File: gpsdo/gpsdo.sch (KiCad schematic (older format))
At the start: 1 part

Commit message: main
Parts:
- added C? (x11): 100n, Capacitor_SMD:C_0402_1005Metric, symbol pace:100n
- added C? (x2): 10u, Capacitor_SMD:C_0402_1005Metric, symbol pace:10u
- added F?: fuse-250mA, Fuse:Fuse_1206_3216Metric, symbol pace:fuse-250mA
- added FB? (x2): bead, Inductor_SMD:L_0805_2012Metric, symbol pace:bead
- added H? (x4): MountingHole_Pad, MountingHole:MountingHole_3.2mm_M3_Pad, symbol pace:MountingHole_Pad
- added J?: Barrel_Jack_Switch, Connector_BarrelJack:BarrelJack_Horizontal, symbol pace:Barrel_Jack_Switch
- added J?: USB_B_Micro, Connector_USB:USB_Micro-B_Molex-105017-0001, symbol pace:USB_B_Micro
- added J?: Conn_01x02_Male, symbol Connector:Conn_01x02_Male
- added J?: Conn_02x05_Odd_Even, symbol Connector_Generic:Conn_02x05_Odd_Even
- added R? (x2): 100k, Resistor_SMD:R_0402_1005Metric, symbol pace:100k
- added SW?: pushbutton_switch, Button_Switch_THT:SW_PUSH_6mm, symbol pace:pushbutton_switch
- added SW?: SW_SPDT, pace:Switch_Toggle_ATE1D-2M3-10-Z, symbol pace:SW_SPDT
- added U?: AP1117-33, Package_TO_SOT_SMD:SOT-223-3_TabPin2, symbol pace:AP1117-33
- added U?: SRV05-4, Package_TO_SOT_SMD:SOT-23-6, symbol pace:SRV05-4
- added U?: 74AHC1G04, Package_TO_SOT_SMD:SOT-353_SC-70-5, symbol pace:74AHC1G04
- added X?: AOCJY1-10.000MHZ, Oscillator:Oscillator_DIP-14, symbol pace:AOCJY1-10.000MHZ
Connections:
- net GND: now reaches U?.10 (VSS)
- net GND: now also U?.20 (VSSA), U?.27 (VSS), U?.74 (VSS), U?.99 (VSS), C?.2, C?.2, C?.2, C?.2, C?.2, C?.2, C?.2, C?.2, C?.2, C?.2, C?.2, C?.2, C?.2, H?.1, H?.1, H?.1, H?.1, J?.1 (Pin_1), J?.2, J?.3, J?.5 (GND), R?.2, SW?.1, U?.1 (GND), U?.2 (VN), U?.3 (GND), X?.7 (GND)
- net +3V3: now reaches U?.100 (VDD)
- net +3V3: now also U?.11 (VDD), U?.19 (VDD), U?.28 (VDD), U?.50 (VDD), U?.6 (VBAT), U?.75 (VDD), C?.1, C?.1, C?.1, C?.1, C?.1, C?.1, C?.1, C?.1, C?.1, C?.1, FB?.1, U?.2 (VO), U?.5 (VCC), X?.14 (Vcc)
- net at U?.22 (VDDA): now also C?.1, FB?.2
- new net: J?.1, SW?.2 (B)
- new net: F?.2, SW?.1 (A)
- new net: C?.1, FB?.1, U?.3 (VI)
- new net: F?.1, FB?.2
- new net: J?.2 (Pin_2), U?.4
- new net OSC_10MHZ: U?.2, X?.8 (OUT)
- new net OSC_CONTROL: X?.1 (Vcontrol)
- new net USB_DM: J?.2 (D-), U?.3 (IO2)
- new net USB_DP: J?.3 (D+), U?.1 (IO1)
- new net VUSB: J?.1 (VBUS), R?.1, U?.5 (VP)
- new net VUSB_SENSE: R?.1, R?.2
- new net nRESET: C?.1, SW?.2
- no-connect marks 0 -> 4
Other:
- moved on the sheet: U?

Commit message: layout
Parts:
- added AE1: Antenna_Shield, pace:sma, symbol Device:Antenna_Shield
- added C10, C15: 100n, Capacitor_SMD:C_0402_1005Metric, symbol pace:100n
- added C16, C17: 2.2uF, Capacitor_SMD:C_0603_1608Metric, symbol pace:2.2uF
- added D1: ledgreen, LED_SMD:LED_0603_1608Metric, symbol pace:ledgreen
- added D2: SS210, Diode_SMD:D_SMA, symbol pace:SS210
- added J3: Conn_01x04_Male, Connector_PinHeader_2.54mm:PinHeader_1x04_P2.54mm_Vertical, symbol Connector:Conn_01x04_Male
- added J6: Conn_01x06_Male, Connector_PinHeader_2.54mm:PinHeader_1x06_P2.54mm_Vertical, symbol Connector:Conn_01x06_Male
- added L1: 47nH, Inductor_SMD:L_0603_1608Metric, symbol pace:47nH
- added R1, R2, R3, R4, R5, R6: 10k, Resistor_SMD:R_0402_1005Metric, symbol pace:10k
- added TH1: 47k, Resistor_SMD:R_0603_1608Metric, symbol pace:47k
- added TP1, TP2, TP3: TestPoint, TestPoint:TestPoint_Pad_D1.0mm, symbol pace:TestPoint
- added U2: ATGM336H-5N, pace:module18_9.7x10.1mm_P1.1mm, symbol pace:ATGM336H-5N
- J1: renamed from J?; footprint (none) -> Connector_PinHeader_1.27mm:PinHeader_2x05_P1.27mm_Vertical
- J5: renamed from J?; footprint (none) -> Connector_PinHeader_2.54mm:PinHeader_1x02_P2.54mm_Vertical
- gave numbers to parts that had none: 31
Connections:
- net +3V3: now also J1.1 (Pin_1), C15.1, J3.2 (Pin_2), R2.1, R3.1, R4.1, U2.8 (VCC)
- net GND: now also J1.3 (Pin_3), J1.5 (Pin_5), J1.9 (Pin_9), AE1.2 (Shield), C10.2, C15.2, C16.2, C17.2, D1.1 (K), J3.1 (Pin_1), J6.1 (Pin_1), R1.2, TH1.2, U2.1 (GND), U2.10 (GND), U2.12 (GND)
- net OSC_10MHZ: now also U1.12 (PH0), U1.31 (PA6), U1.40 (PE9), TP2.1
- net OSC_CONTROL: now also U1.29 (PA4), R6.1, TP1.1; no longer X1.1 (Vcontrol)
- net USB_DM: now also U1.70 (PA11)
- net USB_DP: now also U1.71 (PA12)
- net VUSB_SENSE: now also U1.68 (PA9)
- net nRESET: now also J1.10 (Pin_10), U1.14 (NRST)
- net GPS_1PPS: now reaches U1.32 (PA7)
- net GPS_1PPS: now also U1.42 (PE11), TP3.1, U2.4 (1PPS)
- net GPS_ONOFF: now reaches U1.35 (PB0)
- net GPS_ONOFF: now also U2.5 (ONOFF)
- net GPS_nRESET: now reaches U1.36 (PB1)
- net GPS_nRESET: now also U2.9 (nRESET)
- net LED_STATUS: now reaches U1.37 (PB2)
- net LED_STATUS: now also R5.1
- net CPU_TO_GPS: now reaches U1.47 (PB10)
- net CPU_TO_GPS: now also U2.3 (RXD)
- net GPS_TO_CPU: now reaches U1.48 (PB11)
- net GPS_TO_CPU: now also U2.2 (TXD)
- net at U1.49 (VCAP_1): now also C16.1
- net CPU_TO_AUX: now reaches U1.63 (PC6)
- net CPU_TO_AUX: now also J6.5 (Pin_5)
- net AUX_TO_CPU: now reaches U1.64 (PC7)
- net AUX_TO_CPU: now also J6.4 (Pin_4)
- net SWDIO: now reaches U1.72 (PA13)
- net SWDIO: now also J1.2 (Pin_2)
- net at U1.73 (VCAP_2): now also C17.1
- net SWDCLK: now reaches U1.76 (PA14)
- net SWDCLK: now also J1.4 (Pin_4)
- net SWO: now reaches U1.89 (PB3)
- net SWO: now also J1.6 (Pin_6)
- net SDA: now reaches U1.93 (PB7)
- net SDA: now also J3.4 (Pin_4), R3.2, U2.16 (SDA)
- net BOOT0: now reaches U1.94 (BOOT0)
- net BOOT0: now also R1.1
- net SCL: now reaches U1.95 (PB8)
- net SCL: now also J3.3 (Pin_3), R2.2, U2.17 (SCL)
- net at J2.1: now also D2.2 (A); no longer SW2.2 (B)
- new net: AE1.1 (A), L1.2, U2.11 (RF_IN)
- new net: L1.1, U2.14 (VCC_RF)
- new net: C10.1, R6.2, X1.1 (Vcontrol)
- new net: D2.1 (K), SW2.2 (B)
- new net: D1.2 (A), R5.2
- new net BOARD_TEMP: R4.2, TH1.1
- no-connect marks 4 -> 73
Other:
- note added: "5..12v"
- note added: "Max input 15v"
- note added: "TC = 1 msec"
- moved on the sheet: C12, C14, J1, J2, J4, J5, R7, R8, U4, U5, X1

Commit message: layout
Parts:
- removed D1: ledgreen, LED_SMD:LED_0603_1608Metric, symbol pace:ledgreen
- removed J3: Conn_01x04_Male, Connector_PinHeader_2.54mm:PinHeader_1x04_P2.54mm_Vertical, symbol Connector:Conn_01x04_Male
- removed J6: Conn_01x06_Male, Connector_PinHeader_2.54mm:PinHeader_1x06_P2.54mm_Vertical, symbol Connector:Conn_01x06_Male
- removed U4: 74AHC1G04, Package_TO_SOT_SMD:SOT-353_SC-70-5, symbol pace:74AHC1G04
- removed U5: SRV05-4, Package_TO_SOT_SMD:SOT-23-6, symbol pace:SRV05-4
- added AE2, AE3, AE4, AE5, AE6, AE7, AE8, AE9: Antenna_Shield, pace:sma, symbol Device:Antenna_Shield
- added C18, C19: 12pf, Capacitor_SMD:C_0402_1005Metric, symbol pace:12pf
- added D1: ledgreen_0805, LED_SMD:LED_0805_2012Metric, symbol pace:ledgreen_0805
- added R9: 220, Resistor_SMD:R_0402_1005Metric, symbol pace:220
- added U4: 74AHC1G04-newfp, pace:SOT-70-dck, symbol pace:74AHC1G04-newfp
- added U5: SRV05-4-newfp, pace:srv05-4, symbol pace:SRV05-4-newfp
- added Y1: 16mhz, Crystal:Crystal_SMD_3225-4Pin_3.2x2.5mm, symbol pace:16mhz
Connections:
- net +3V3: now also U4.5 (VCC)
- net BOARD_TEMP: now also U1.25 (PA2)
- net GND: now also AE2.2 (Shield), AE3.2 (Shield), AE4.2 (Shield), AE5.2 (Shield), AE6.2 (Shield), AE7.2 (Shield), AE8.2 (Shield), AE9.2 (Shield), C18.2, C19.2, D1.1 (K), U4.3 (GND), U5.2 (VN), Y1.2, Y1.4
- net GPS_1PPS: now also U1.69 (PA10); no longer U1.42 (PE11)
- net LED_STATUS: now also U1.26 (PA3); no longer U1.37 (PB2)
- net OSC_10MHZ: now also U1.67 (PA8), U1.90 (PB4), U4.2; no longer U1.12 (PH0), U1.31 (PA6), U1.40 (PE9)
- net USB_DM: now also U5.4 (IO3)
- net USB_DP: now also U5.3 (IO2)
- net VUSB: now also U5.5 (VP)
- net at U1.13 (PH1): now also R9.1
- net at R5.2: now also D1.2 (A)
- net at J5.2 (Pin_2): now also U4.4
- net AUX_TO_CPU: no longer names the net of U1.64 (PC7)
- net CPU_TO_AUX: no longer names the net of U1.63 (PC6)
- new net: C18.1, U1.12 (PH0), Y1.1
- new net: C19.1, R9.2, Y1.3
- new net: AE4.1 (A), AE8.1 (A)
- new net: AE5.1 (A), AE9.1 (A)
- new net: AE3.1 (A), AE7.1 (A)
- new net: AE2.1 (A), AE6.1 (A)
- no-connect marks 73 -> 70
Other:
- note added: "use JLC7628 ; 50 ohm trace = 11.55 mil"
- moved on the sheet: AE1, C15, L1, U2

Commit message: rotate
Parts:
- U5: footprint pace:srv05-4 -> pace:SOT-23-6L-srv05
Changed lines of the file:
@@
 F 0 "U5" H 8650 2631 50  0000 C CNN
 F 1 "SRV05-4-newfp" H 8650 2540 50  0000 C CNN
-F 2 "pace:srv05-4" H 9350 1500 50  0001 C CNN
+F 2 "pace:SOT-23-6L-srv05" H 9350 1500 50  0001 C CNN
 F 3 "http://www.onsemi.com/pub/Collateral/SRV05-4-D.PDF" H 8650 1950 50  0001 C CNN
 F 4 "C85364" H 8650 1950 50  0001 C CNN "LCSC"

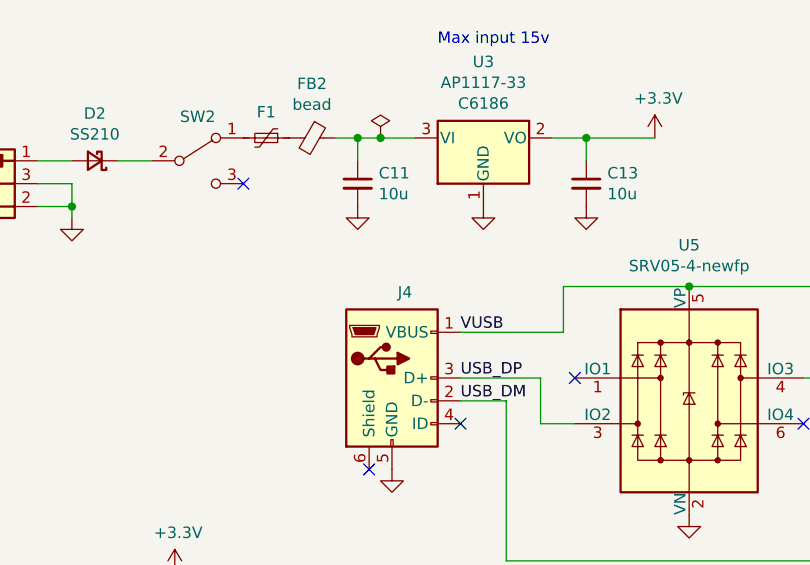
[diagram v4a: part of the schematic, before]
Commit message: usb connector
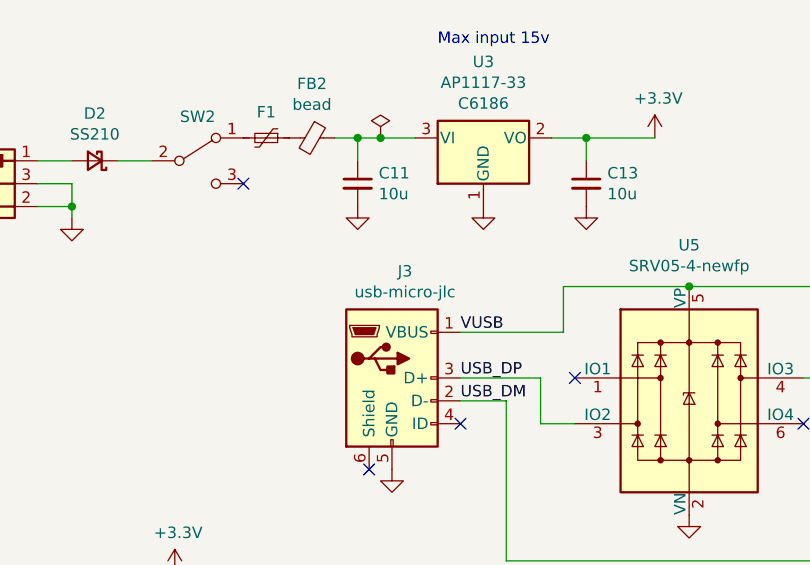
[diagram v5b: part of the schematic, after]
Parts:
- removed J4: USB_B_Micro, Connector_USB:USB_Micro-B_Molex-105017-0001, symbol pace:USB_B_Micro
- added J3: usb-micro-jlc, pace:usb-micro-jlc, symbol pace:usb-micro-jlc
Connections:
- net GND: now also J3.5 (GND)
- net USB_DM: now also J3.2 (D-)
- net USB_DP: now also J3.3 (D+)
- net VUSB: now also J3.1 (VBUS)
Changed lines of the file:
@@
-	1    0    0    -1
-$EndComp
-$Comp
-L pace:USB_B_Micro J4
-U 1 1 60403348
-P 7350 1850
-F 0 "J4" H 7407 2225 50  0000 C CNN
-F 1 "USB_B_Micro" H 7150 2200 50  0001 L CNN
-F 2 "Connector_USB:USB_Micro-B_Molex-105017-0001" H 7500 1800 50  0001 C CNN
-F 3 "~" H 7500 1800 50  0001 C CNN
-	1    7350 1850
 	1    0    0    -1
 $EndComp
@@
 Text Label 3850 2150 0    50   ~ 0
 BOARD_TEMP
+$Comp
+L pace:usb-micro-jlc J3
+U 1 1 603DB4F9
+P 7350 1850
+F 0 "J3" H 7407 2317 50  0000 C CNN
+F 1 "usb-micro-jlc" H 7407 2226 50  0000 C CNN
+F 2 "pace:usb-micro-jlc" H 7500 1800 50  0001 C CNN
+F 3 "https://lcsc.com/product-detail/USB-Connectors_SHOU-HAN-MicroXNJ_C404969.html/?href=jlc-SMT" H 7500 1800 50  0001 C CNN
+F 4 "C404969" H 7350 1850 50  0001 C CNN "LCSC"
+	1    7350 1850
+	1    0    0    -1
+$EndComp
 $EndSCHEMATC
